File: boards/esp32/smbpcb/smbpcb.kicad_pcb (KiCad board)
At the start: 2 copper layers, 85.4 x 70.4 mm, 74 parts, among them IC1 MiCS-6814, J1 USB_B_Micro, J2 PMS7003, Q1 SUD08P06-155L, Q2 SS8050_NPN, Q3 SS8050_NPN, SW1 RESET, SW2 RESET, U1 MCP73831-2-OT, U2 TPS61200DRC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

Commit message: tidied up
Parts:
- moved C7 2.04 mm to (91.7, 47.5), turned to 90 degrees
- moved R21 1.94 mm to (100.1, 39.6)
- moved R7 1.71 mm to (89.5, 47.5)
- moved R11 1.47 mm to (78.5, 76.5), turned to 180 degrees
- moved C10 1.30 mm to (105.6, 43.6)
- moved R12 1.14 mm to (82.7, 80.5)
- moved C6 1.00 mm to (101.4, 43.6)
- moved R10 0.72 mm to (60.9, 54.3)
- moved C8 0.56 mm to (103.5, 43.6)
- moved R28 0.48 mm to (44.1, 56.9)
- moved C15 0.40 mm to (61.4, 69.4)
- moved D4 0.21 mm to (40.5, 56.9)
- moved C14 0.17 mm to (105.7, 37.7)
- moved R17 0.14 mm to (98.7, 48.5)
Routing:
- net +3V3: track 213.6 -> 219.5 mm
- net Net-(Q2-Pad3): track 13.5 -> 19.3 mm, vias 2 -> 0
- net Net-(C7-Pad1): track 5.48 -> 10.7 mm
- net ESP_RX1: track 8.05 -> 4.31 mm
- net ESP_RX0: track 25.1 -> 22.6 mm, vias 3 -> 2
- net GND: track 171.1 -> 173.5 mm
- net Net-(C3-Pad1): track 22.0 -> 23.6 mm
- net Net-(R21-Pad2): track 2.97 -> 4.43 mm
- net Net-(R7-Pad2): track 10.6 -> 11.7 mm
- net Net-(C7-Pad2): track 6.77 -> 7.62 mm
- net Net-(C1-Pad1): track 28.0 -> 27.3 mm
- net Net-(J1-Pad2): track 0.00 -> 0.65 mm
- net Net-(C15-Pad2): track 4.76 -> 4.13 mm
- net Net-(C6-Pad2): track 4.47 -> 5.11 mm
- net +5V: track 45.0 -> 44.4 mm
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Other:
- board text added: "DIYAQI Cluster Board"

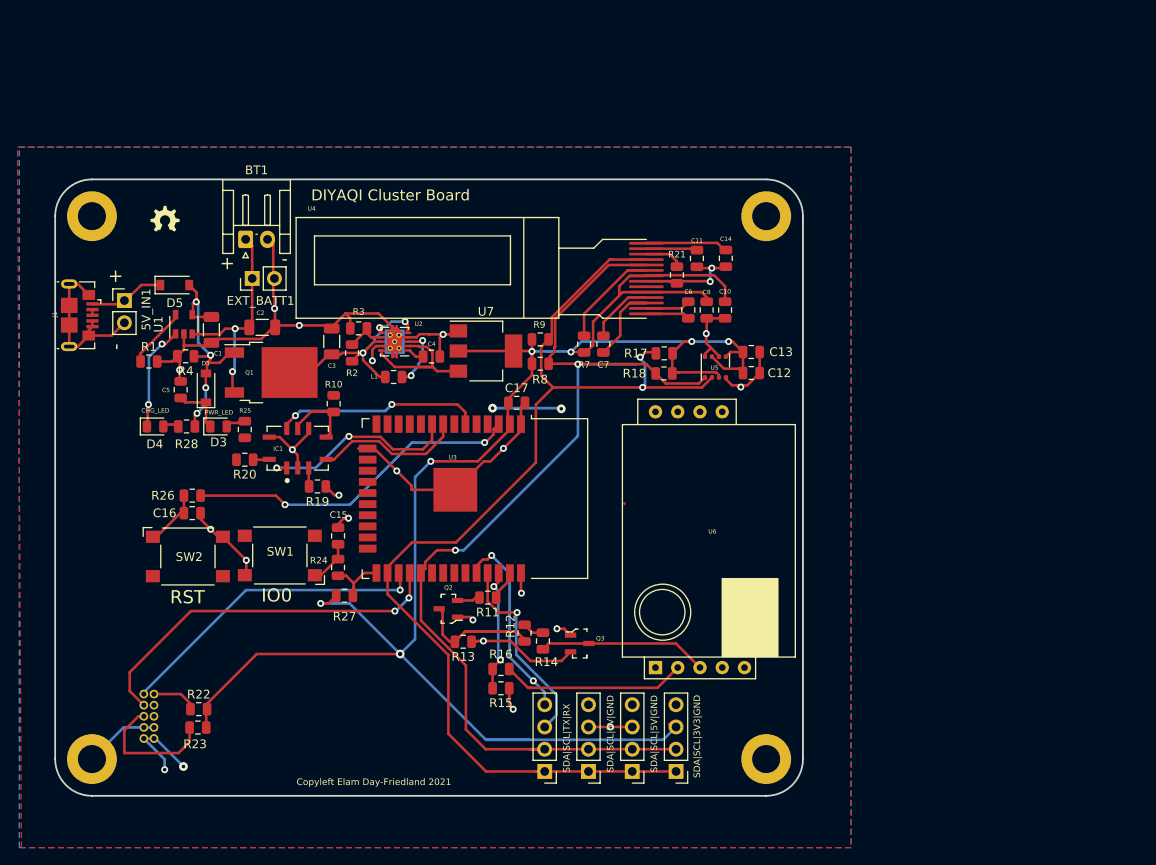
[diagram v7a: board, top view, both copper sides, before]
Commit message: more tidying and controled impedence traces for important stuff
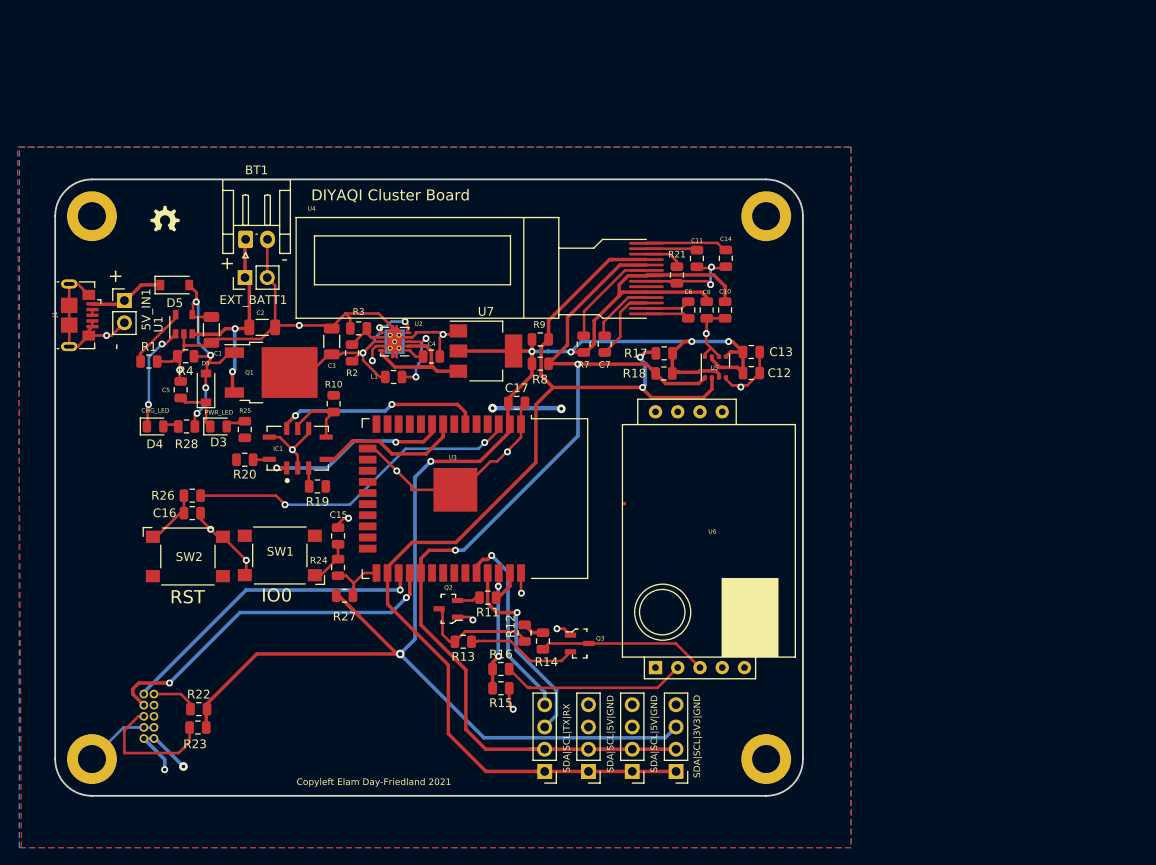
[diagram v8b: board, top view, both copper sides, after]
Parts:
- moved EXT_BATT1 0.83 mm to (50.8, 39.9)
- moved C7 0.15 mm to (91.8, 47.5)
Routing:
- net SCL: track 124.0 -> 117.4 mm
- net +3V3: track 219.5 -> 213.1 mm, vias 7 -> 6
- net +5V: track 44.4 -> 38.0 mm, vias 6 -> 4
- net SDA: track 129.1 -> 130.9 mm
- net ESP_RX2: track 42.7 -> 40.9 mm
- net Net-(L1-Pad2): track 7.72 -> 8.95 mm
- net ESP_RX1: track 4.31 -> 5.27 mm
- net NO2: track 23.3 -> 22.7 mm
- net ESP_TX1: track 14.1 -> 13.5 mm
- net Net-(Q3-Pad2): vias 1 -> 0
- net ESP_RX0: vias 2 -> 1
